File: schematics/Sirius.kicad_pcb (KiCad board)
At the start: 2 copper layers, 14 parts, among them J1 DE9_Plug, U1 W65C02SxP, U10 MAX232, U11 7404, U2 W65C51NxP, U3 2764, U4 74LS138, U5 74LS138, X1 TFT680, X2 TFT680

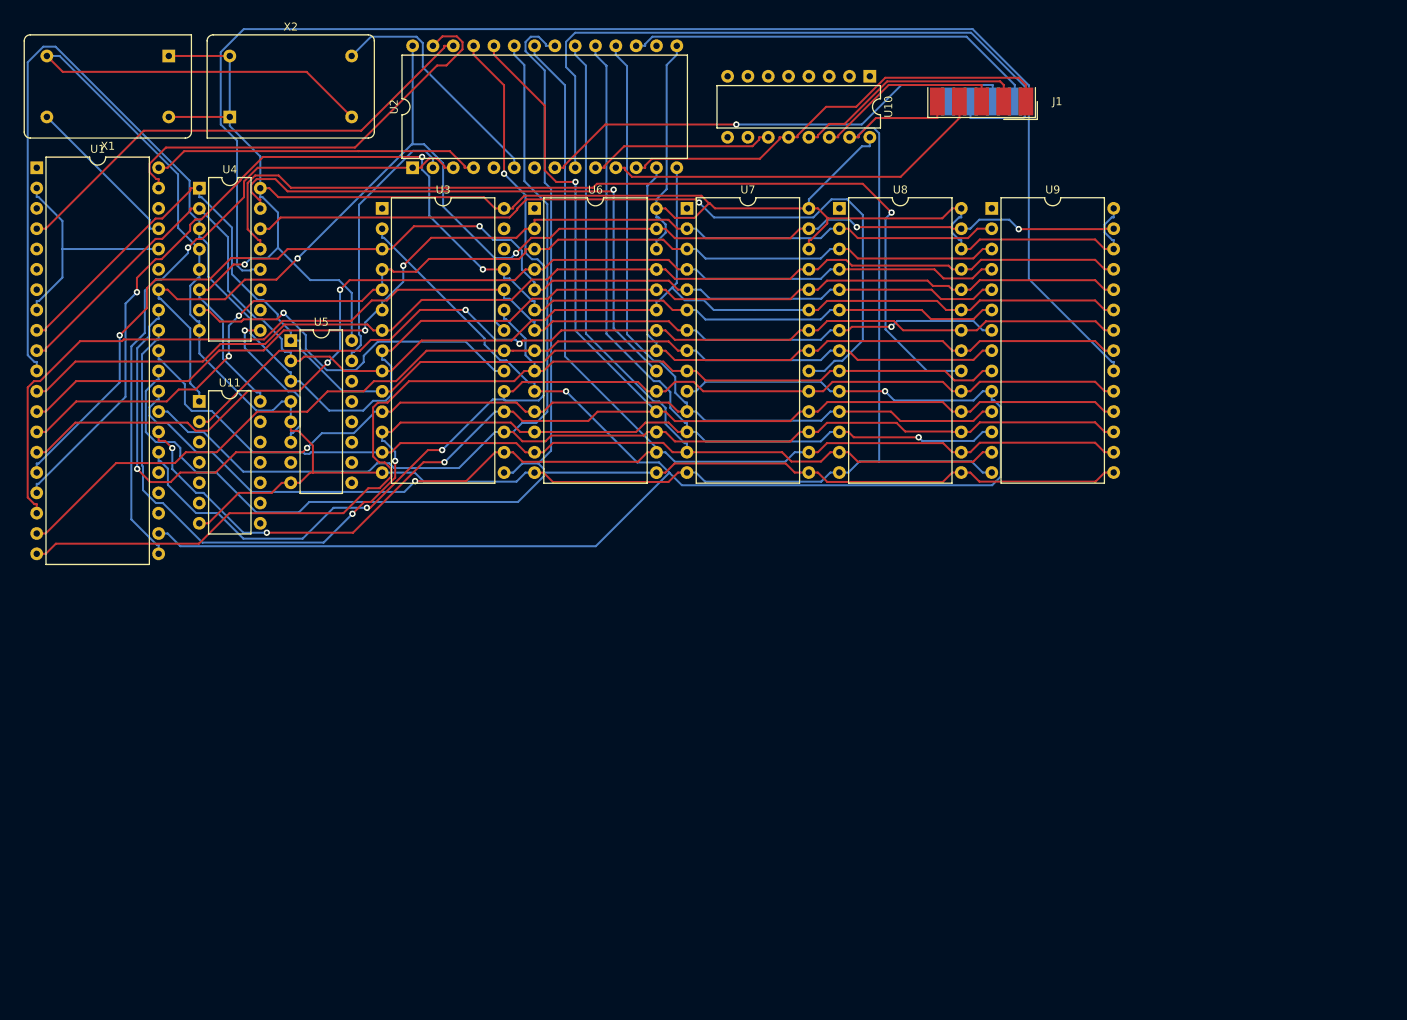
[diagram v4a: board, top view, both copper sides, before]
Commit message: Minor alterations to PCB layout.
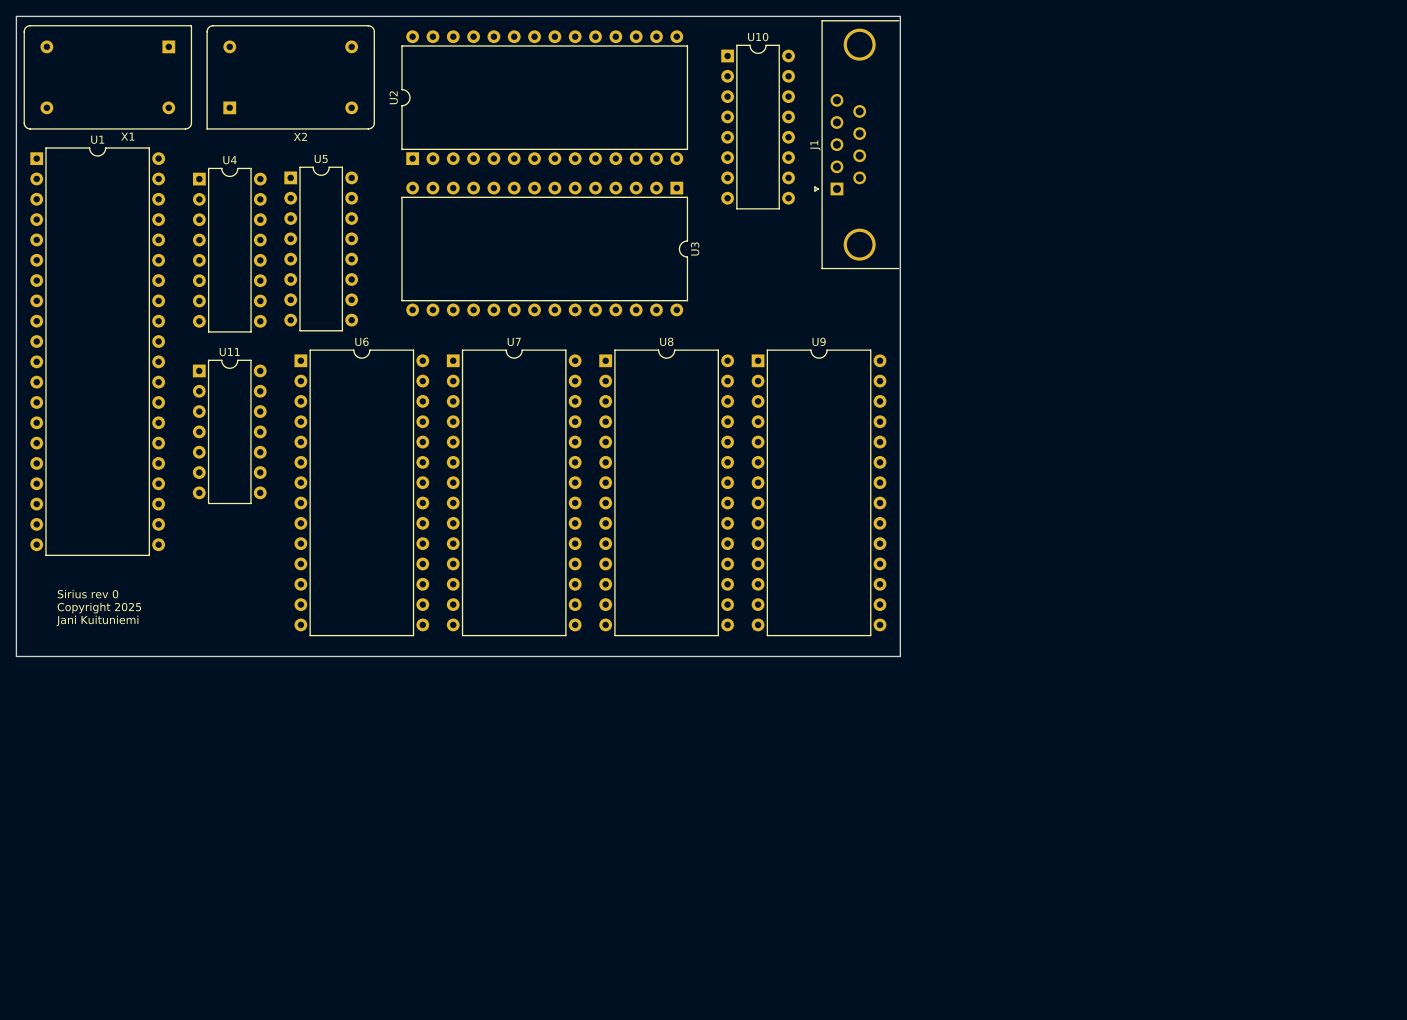
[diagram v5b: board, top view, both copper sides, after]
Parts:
- J1: footprint Connector_Dsub:DSUB-9_Male_EdgeMount_P2.77mm -> Connector_Dsub:DSUB-9_Male_Horizontal_P2.77x2.84mm_EdgePinOffset4.94mm_Housed_MountingHolesOffset4.94mm
- moved U3 36.9 mm to (94.0, 33.0), turned to -90 degrees
- moved U7 34.9 mm to (66.0, 54.6)
- moved U8 34.9 mm to (85.1, 54.6)
- moved U9 34.9 mm to (104.1, 54.6)
- moved U6 34.9 mm to (47.0, 54.6)
- moved J1 21.1 mm to (114.0, 33.1), turned to 90 degrees
- moved U5 20.3 mm to (45.7, 31.8)
- moved U10 18.0 mm to (100.3, 16.5), turned to 0 degrees
- moved U11 3.81 mm to (34.3, 55.9)
- moved X1 1.14 mm to (30.5, 15.4)
- moved U1 1.14 mm to (14.0, 29.3)
- moved U2 1.14 mm to (61.0, 29.3)
- moved X2 1.14 mm to (38.1, 23.0)
- moved U4 1.14 mm to (34.3, 31.9)
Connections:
- U1 pad 3: unconnected-(U1-ϕ1-Pad3) -> (no net)
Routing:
- net GND: track 279.4 -> 0.00 mm
- net VCC: track 265.8 -> 0.00 mm, vias 1 -> 0
- net A2: track 216.5 -> 0.00 mm
- net A12: track 212.5 -> 0.00 mm, vias 2 -> 0
- net /D3: track 204.8 -> 0.00 mm
- net /D1: track 198.8 -> 0.00 mm, vias 3 -> 0
- net /D6: track 192.5 -> 0.00 mm, vias 4 -> 0
- net /D4: track 191.4 -> 0.00 mm, vias 1 -> 0
- net /D7: track 190.8 -> 0.00 mm, vias 3 -> 0
- net A0: track 187.4 -> 0.00 mm
- net /D0: track 186.2 -> 0.00 mm, vias 2 -> 0
- net /D5: track 182.8 -> 0.00 mm
- net A1: track 179.7 -> 0.00 mm
- net Net-(U1-R/~{W}): track 179.4 -> 0.00 mm, vias 4 -> 0
- net Net-(U4-O3): track 176.1 -> 0.00 mm
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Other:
- board outline added: 110.5 x 80 mm
- board text added: "Sirius rev 0 Copyright 2025 Jani Kuituniemi"

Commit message: Some ERC and DRC fixes.
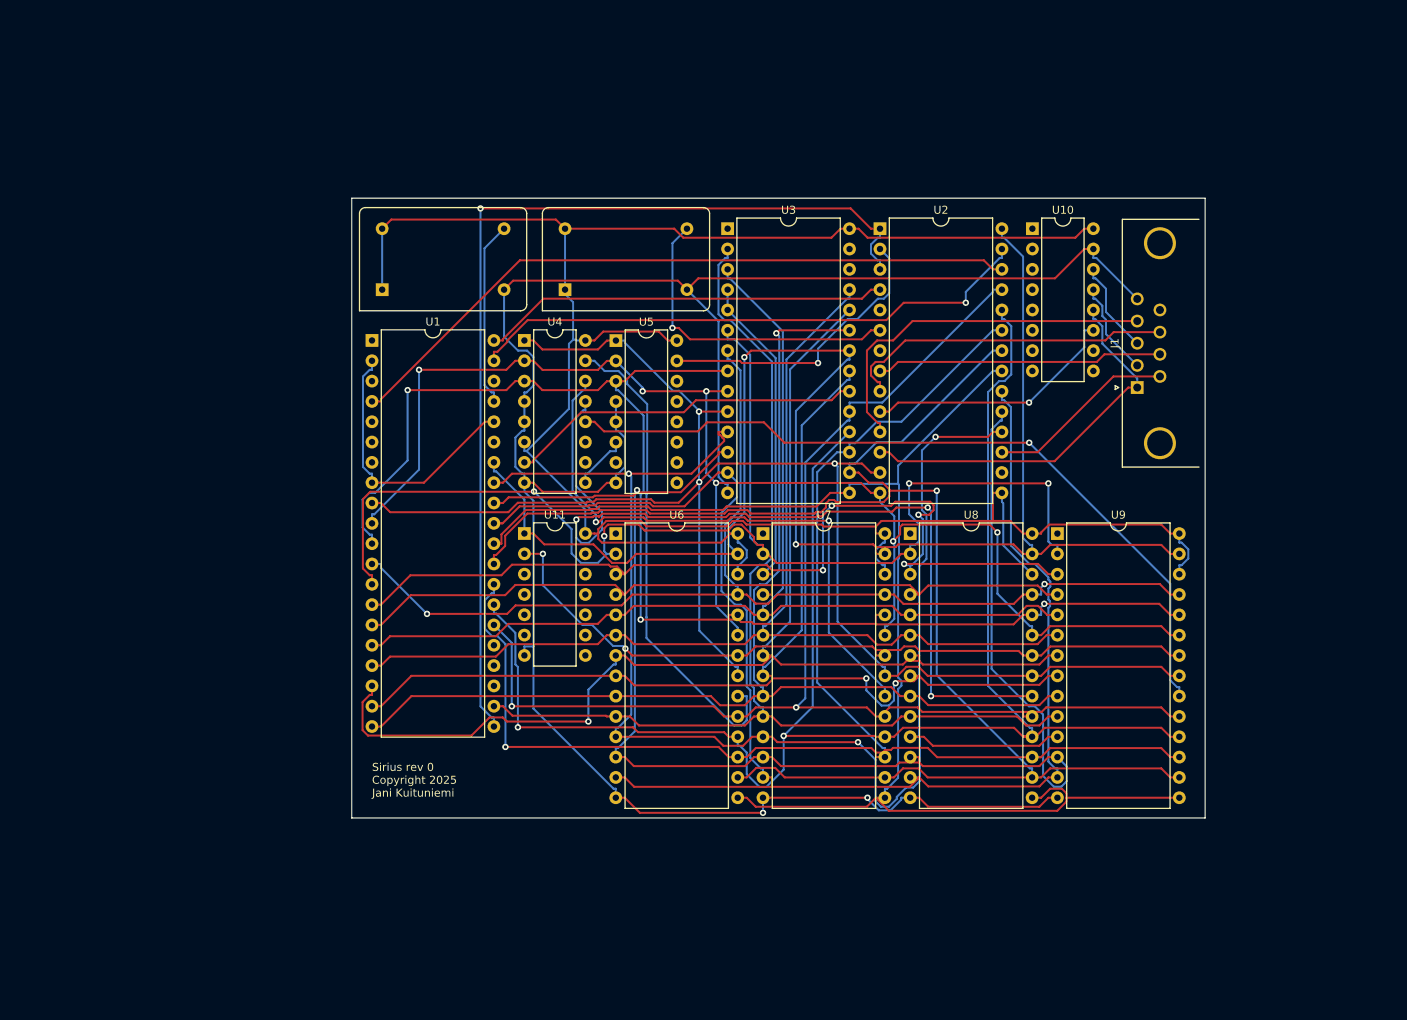
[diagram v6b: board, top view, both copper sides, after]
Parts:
- moved U2 59.1 mm to (119.4, 38.1), turned to 0 degrees
- moved U1 47.7 mm to (55.9, 52.1)
- moved X2 47.7 mm to (80.0, 45.7)
- moved U5 45.5 mm to (86.4, 52.1)
- moved U11 45.4 mm to (74.9, 76.2)
- moved U4 45.4 mm to (74.9, 52.1)
- moved J1 45.0 mm to (151.5, 58.0)
- moved U6 44.9 mm to (86.4, 76.2)
- moved U7 44.3 mm to (104.8, 76.2)
- moved U10 43.8 mm to (138.4, 38.1)
- moved U8 43.8 mm to (123.2, 76.2)
- moved U9 43.2 mm to (141.6, 76.2)
- moved X1 40.4 mm to (57.1, 45.7), turned to 0 degrees
- moved U3 8.13 mm to (100.3, 38.1), turned to 0 degrees
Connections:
- U2 pad 16: unconnected-(U2-~{DCD}-Pad16) -> Net-(U10-R1OUT)
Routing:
- net VCC: track 0.00 -> 292.7 mm
- net GND: track 0.00 -> 272.0 mm, vias 0 -> 2
- net /D6: track 0.00 -> 212.4 mm, vias 0 -> 2
- net A0: track 0.00 -> 200.7 mm, vias 0 -> 3
- net Net-(U1-R/~{W}): track 0.00 -> 200.0 mm, vias 0 -> 2
- net /D4: track 0.00 -> 193.3 mm, vias 0 -> 1
- net /D0: track 0.00 -> 188.0 mm, vias 0 -> 3
- net /D2: track 0.00 -> 187.1 mm
- net A1: track 0.00 -> 185.0 mm, vias 0 -> 6
- net /D5: track 0.00 -> 182.8 mm, vias 0 -> 1
- net /D1: track 0.00 -> 182.7 mm, vias 0 -> 1
- net /D3: track 0.00 -> 180.4 mm
- net A2: track 0.00 -> 169.8 mm, vias 0 -> 3
- net /D7: track 0.00 -> 165.8 mm, vias 0 -> 2
- net A4: track 0.00 -> 163.3 mm, vias 0 -> 4
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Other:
- board size 110.5 x 80 mm -> 106.7 x 77.5 mm
